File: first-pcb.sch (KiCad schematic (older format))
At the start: 14 parts

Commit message: Electronic schematic is over
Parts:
- added D1, D2, D3, D4: D_Small, Diode_SMD:D_SOD-123, symbol Device:D_Small
- added F1: 500mA, Fuse:Fuse_1206_3216Metric, symbol Device:Polyfuse
- added MX1, MX2, MX3, MX4: MX-NoLED, MX_Alps_Hybrid:MX-1U-NoLED, symbol MX_Alps_Hybrid:MX-NoLED
- added USB1: Molex-0548190589, random-keyboard-parts:Molex-0548190589, symbol random-keyboard-parts:Molex-0548190589
- C1, C2, C3, C4, C5, C6: renamed from C?; footprint (none) -> Capacitor_SMD:C_0805_2012Metric
- C7: renamed from C?; footprint (none) -> Diode_SMD:D_SOD-123
- R1, R2, R3, R4: renamed from R?; footprint (none) -> Resistor_SMD:R_0805_2012Metric
- SW1: renamed from SW?; footprint (none) -> random-keyboard-parts:SKQG-1155865
- Y1: renamed from Y?; footprint (none) -> Crystal:Crystal_SMD_3225-4Pin_3.2x2.5mm
- gave numbers to parts that had none: 1
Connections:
- net +5V: now also F1.1
- net D+: now also USB1.3 (D+)
- net D-: now also USB1.4 (D-)
- net GND: now also USB1.1 (GND)
- new net: D1.2 (A), MX1.2 (ROW)
- new net: D3.2 (A), MX3.2 (ROW)
- new net: D2.2 (A), MX2.2 (ROW)
- new net: D4.2 (A), MX4.2 (ROW)
- new net COL0: MX1.1 (COL), MX2.1 (COL)
- new net COL1: MX3.1 (COL), MX4.1 (COL)
- new net ROW0: D1.1 (K), D3.1 (K)
- new net ROW1: D2.1 (K), D4.1 (K)
- new net VCC: F1.2, USB1.5 (VBUS)

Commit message: My very first pcb is over
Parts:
- renumbered D3 to D2, D2 to D3, MX3 to MX2, MX2 to MX3
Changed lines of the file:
@@
 	6550 3600 6700 3600
 $Comp
-L MX_Alps_Hybrid:MX-NoLED MX3
+L MX_Alps_Hybrid:MX-NoLED MX2
 U 1 1 5E8CAD05
 P 7400 3450
-F 0 "MX3" H 7433 3673 60  0000 C CNN
+F 0 "MX2" H 7433 3673 60  0000 C CNN
 F 1 "MX-NoLED" H 7433 3599 20  0000 C CNN
 F 2 "MX_Alps_Hybrid:MX-1U-NoLED" H 6775 3425 60  0001 C CNN
@@
 $EndComp
 $Comp
-L Device:D_Small D3
+L Device:D_Small D2
 U 1 1 5E8CAD0B
 P 7200 3700
-F 0 "D3" V 7246 3630 50  0000 R CNN
+F 0 "D2" V 7246 3630 50  0000 R CNN
 F 1 "D_Small" V 7155 3630 50  0000 R CNN
 F 2 "Diode_SMD:D_SOD-123" V 7200 3700 50  0001 C CNN
@@
 	7200 3600 7350 3600
 $Comp
-L MX_Alps_Hybrid:MX-NoLED MX2
+L MX_Alps_Hybrid:MX-NoLED MX3
 U 1 1 5E8CBEF5
 P 6750 4150
-F 0 "MX2" H 6783 4373 60  0000 C CNN
+F 0 "MX3" H 6783 4373 60  0000 C CNN
 F 1 "MX-NoLED" H 6783 4299 20  0000 C CNN
 F 2 "MX_Alps_Hybrid:MX-1U-NoLED" H 6125 4125 60  0001 C CNN
@@
 $EndComp
 $Comp
-L Device:D_Small D2
+L Device:D_Small D3
 U 1 1 5E8CBEFB
 P 6550 4400
-F 0 "D2" V 6596 4330 50  0000 R CNN
+F 0 "D3" V 6596 4330 50  0000 R CNN
 F 1 "D_Small" V 6505 4330 50  0000 R CNN
 F 2 "Diode_SMD:D_SOD-123" V 6550 4400 50  0001 C CNN

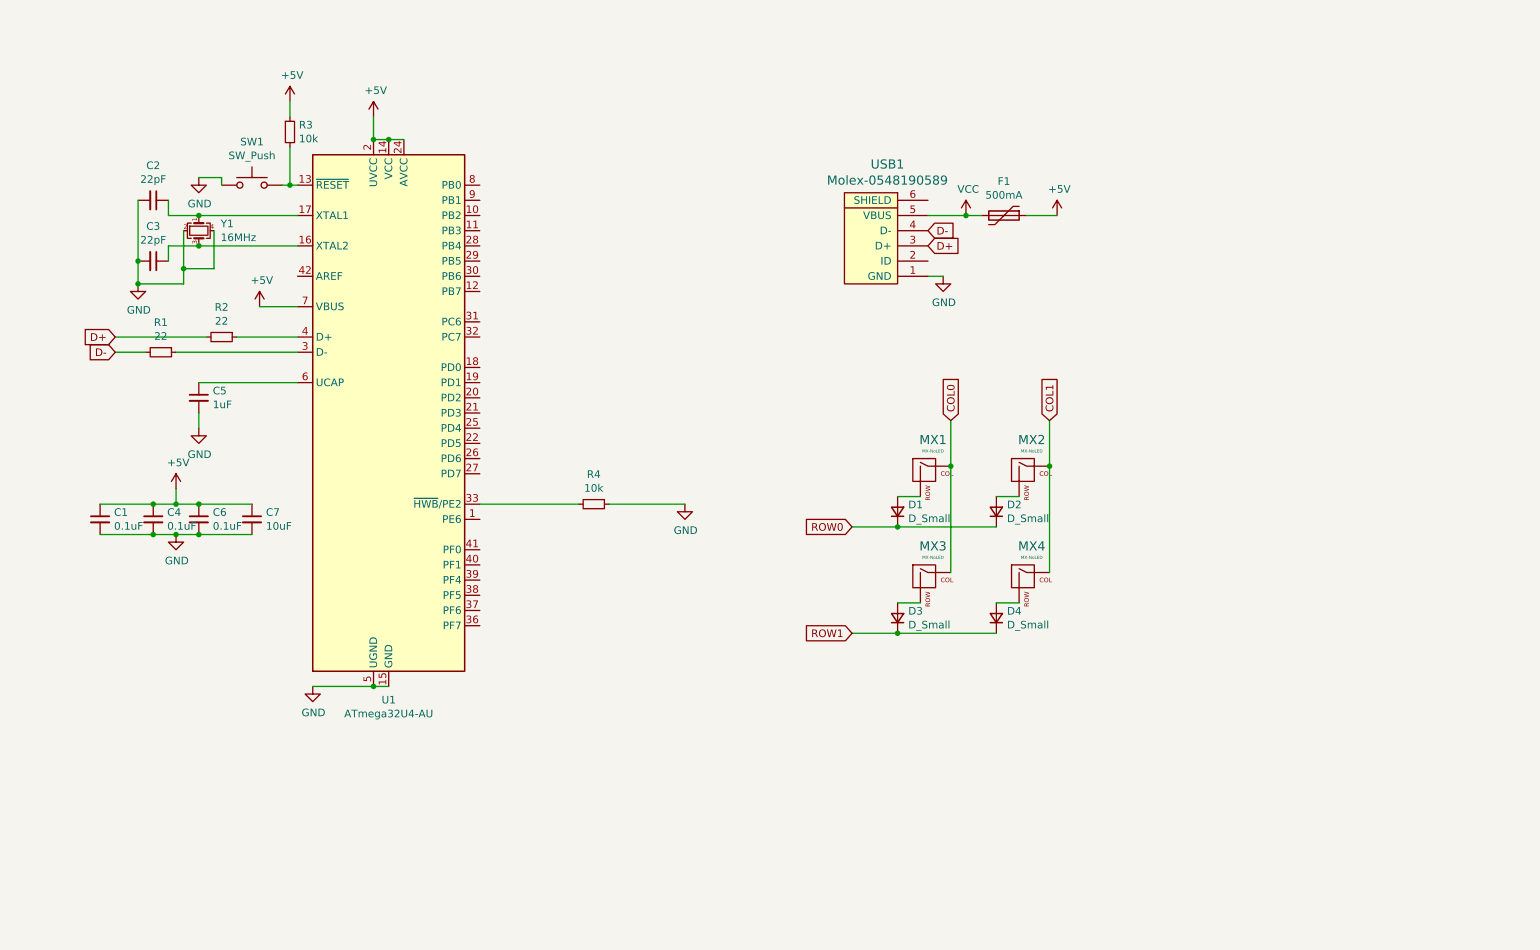
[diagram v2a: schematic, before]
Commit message: First revision (#1)
First design includes 44 switch, 44 smd diodes, 1 pro-micro, 1 4-pin header for oled screen,
outline and mounting points

* V0.0.1 of the flatbrain keyboard

* Replace 1u in thumb by 1.75 and 1.5

* Perfect alignement

* routing corrected

* realign + outline

* add contour.dxf

* final design

* first revision is over
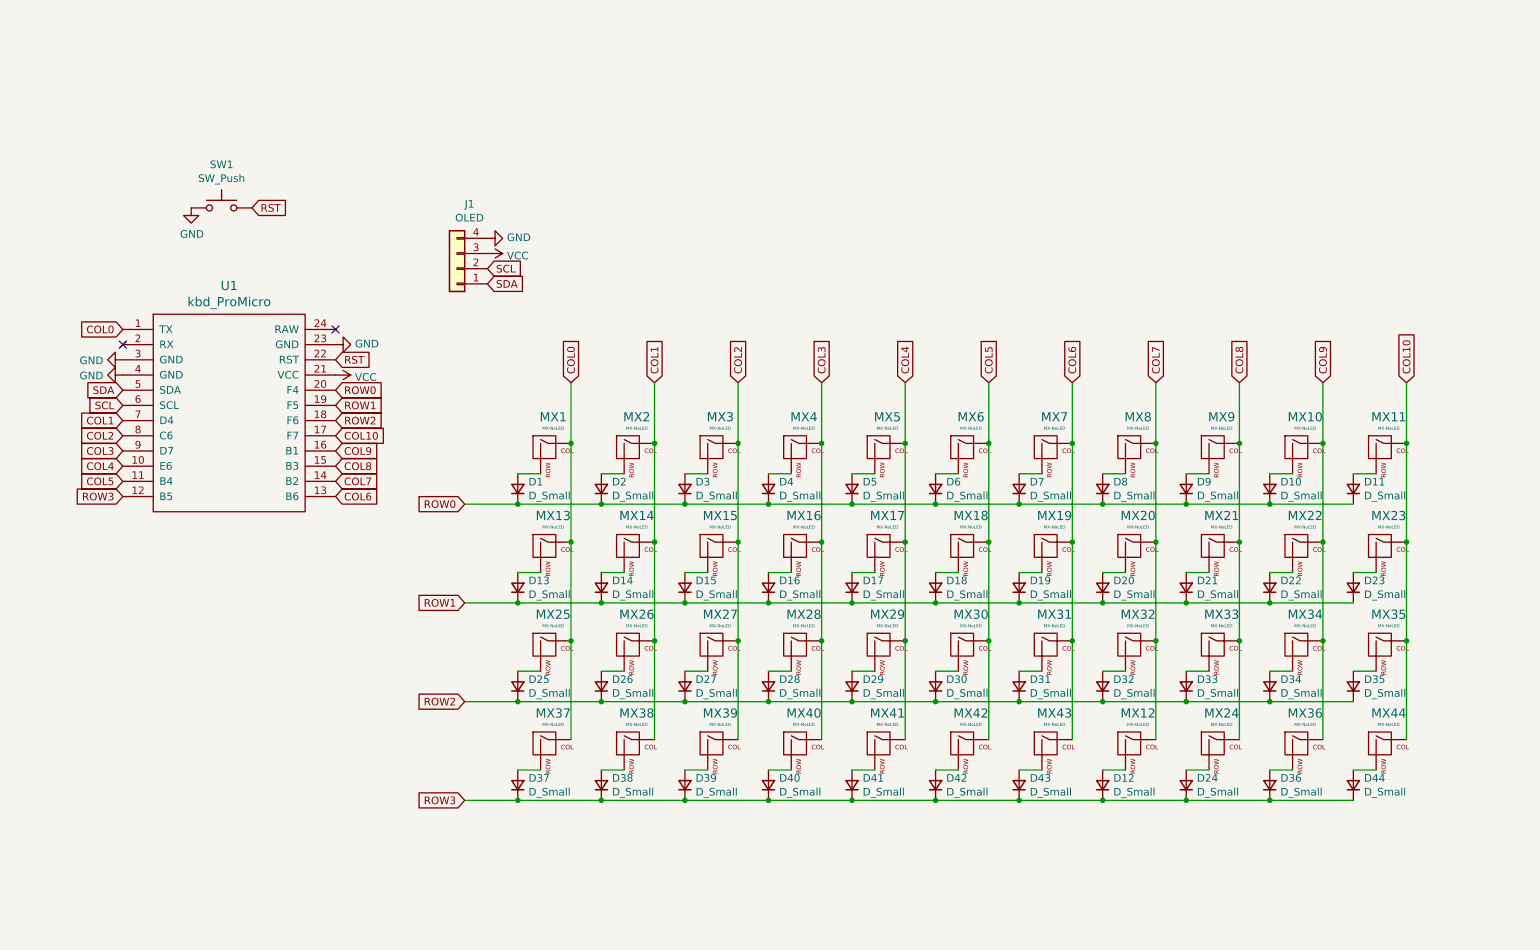
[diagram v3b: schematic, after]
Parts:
- removed C1, C4, C6: 0.1uF, Capacitor_SMD:C_0805_2012Metric, symbol Device:C_Small
- removed C2, C3: 22pF, Capacitor_SMD:C_0805_2012Metric, symbol Device:C_Small
- removed C5: 1uF, Capacitor_SMD:C_0805_2012Metric, symbol Device:C_Small
- removed C7: 10uF, Diode_SMD:D_SOD-123, symbol Device:C_Small
- removed D1: D_Small, Diode_SMD:D_SOD-123, symbol Device:D_Small
- removed F1: 500mA, Fuse:Fuse_1206_3216Metric, symbol Device:Polyfuse
- removed MX1: MX-NoLED, MX_Alps_Hybrid:MX-1U-NoLED, symbol MX_Alps_Hybrid:MX-NoLED
- removed R1, R2: 22, Resistor_SMD:R_0805_2012Metric, symbol Device:R_Small
- removed R3, R4: 10k, Resistor_SMD:R_0805_2012Metric, symbol Device:R_Small
- removed U1: ATmega32U4-AU, Package_QFP:TQFP-44_10x10mm_P0.8mm, symbol MCU_Microchip_ATmega:ATmega32U4-AU
- removed USB1: Molex-0548190589, random-keyboard-parts:Molex-0548190589, symbol random-keyboard-parts:Molex-0548190589
- removed Y1: 16MHz, Crystal:Crystal_SMD_3225-4Pin_3.2x2.5mm, symbol Device:Crystal_GND24_Small
- added D10, D11, D12, D14, D15, D16, D17, D18, D19, D2, D20, D21, D22, D23, D24, D25, D26, D27, D28, D29, D3, D30, D31, D32, D33, D34, D35, D36, D37, D38, D39, D40, D41, D42, D43, D44, D5, D6, D7, D8, D9: D_Small, Diode_SMD:D_SOD-123, symbol Device:D_Small
- added J1: OLED, Connector_PinHeader_2.54mm:PinHeader_1x04_P2.54mm_Vertical, symbol corne-light-cache:Connector_Generic_Conn_01x04
- added MX10, MX11, MX12, MX14, MX15, MX16, MX17, MX18, MX19, MX2, MX20, MX21, MX22, MX23, MX24, MX25, MX26, MX27, MX28, MX29, MX3, MX30, MX31, MX32, MX33, MX34, MX35, MX36, MX37, MX38, MX43, MX44, MX5, MX6, MX7, MX8, MX9: MX-NoLED, MX_Only:MXOnly-1U-NoLED, symbol MX_Alps_Hybrid:MX-NoLED
- added MX39, MX42: MX-NoLED, MX_Only:MXOnly-1.75U-NoLED, symbol MX_Alps_Hybrid:MX-NoLED
- added MX40, MX41: MX-NoLED, MX_Only:MXOnly-1.5U-NoLED, symbol MX_Alps_Hybrid:MX-NoLED
- added U1: kbd_ProMicro, Keebio-Parts:ArduinoProMicro, symbol corne-light-cache:kbd_ProMicro
- MX1: renamed from MX2; footprint MX_Alps_Hybrid:MX-1U-NoLED -> MX_Only:MXOnly-1U-NoLED
- MX13: renamed from MX3; footprint MX_Alps_Hybrid:MX-1U-NoLED -> MX_Only:MXOnly-1U-NoLED
- MX4: footprint MX_Alps_Hybrid:MX-1U-NoLED -> MX_Only:MXOnly-1U-NoLED
- renumbered D2 to D1, D3 to D13
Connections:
- net COL0: now also MX1.1 (COL), MX25.1 (COL), MX37.1 (COL), U1.1 (TX)
- net COL1: now also MX14.1 (COL), MX2.1 (COL), MX26.1 (COL), MX38.1 (COL), U1.7 (D4); no longer MX1.1 (COL), MX4.1 (COL)
- net GND: now also J1.4 (Pin_4), U1.23 (GND), U1.3 (GND), U1.4 (GND)
- net ROW0: now also D4.1 (K), D10.1 (K), D11.1 (K), D2.1 (K), D3.1 (K), D5.1 (K), D6.1 (K), D7.1 (K), D8.1 (K), D9.1 (K), U1.20 (F4)
- net ROW1: now also D14.1 (K), D15.1 (K), D16.1 (K), D17.1 (K), D18.1 (K), D19.1 (K), D20.1 (K), D21.1 (K), D22.1 (K), D23.1 (K), U1.19 (F5); no longer D4.1 (K)
- net VCC: now also J1.3 (Pin_3), U1.21 (VCC)
- net RST: now reaches SW1.2
- net RST: now also U1.22 (RST)
- new net: D2.2 (A), MX2.2 (ROW)
- new net: D3.2 (A), MX3.2 (ROW)
- new net: D14.2 (A), MX14.2 (ROW)
- new net: D15.2 (A), MX15.2 (ROW)
- new net: D5.2 (A), MX5.2 (ROW)
- new net: D16.2 (A), MX16.2 (ROW)
- new net: D17.2 (A), MX17.2 (ROW)
- new net: D25.2 (A), MX25.2 (ROW)
- new net: D26.2 (A), MX26.2 (ROW)
- new net: D27.2 (A), MX27.2 (ROW)
- new net: D28.2 (A), MX28.2 (ROW)
- new net: D29.2 (A), MX29.2 (ROW)
- new net: D30.2 (A), MX30.2 (ROW)
- new net: D6.2 (A), MX6.2 (ROW)
- new net: D18.2 (A), MX18.2 (ROW)
- new net: D37.2 (A), MX37.2 (ROW)
- new net: D38.2 (A), MX38.2 (ROW)
- new net: D39.2 (A), MX39.2 (ROW)
- new net: D40.2 (A), MX40.2 (ROW)
- new net: D7.2 (A), MX7.2 (ROW)
- new net: D19.2 (A), MX19.2 (ROW)
- new net: D8.2 (A), MX8.2 (ROW)
- new net: D9.2 (A), MX9.2 (ROW)
- new net: D20.2 (A), MX20.2 (ROW)
- new net: D21.2 (A), MX21.2 (ROW)
- new net: D10.2 (A), MX10.2 (ROW)
- new net: D11.2 (A), MX11.2 (ROW)
- new net: D22.2 (A), MX22.2 (ROW)
- new net: D23.2 (A), MX23.2 (ROW)
- new net: D31.2 (A), MX31.2 (ROW)
- new net: D32.2 (A), MX32.2 (ROW)
- new net: D33.2 (A), MX33.2 (ROW)
- new net: D34.2 (A), MX34.2 (ROW)
- new net: D35.2 (A), MX35.2 (ROW)
- new net: D36.2 (A), MX36.2 (ROW)
- new net: D12.2 (A), MX12.2 (ROW)
- new net: D24.2 (A), MX24.2 (ROW)
- new net: D41.2 (A), MX41.2 (ROW)
- new net: D42.2 (A), MX42.2 (ROW)
- new net: D43.2 (A), MX43.2 (ROW)
- new net: D44.2 (A), MX44.2 (ROW)
- new net COL10: MX11.1 (COL), MX23.1 (COL), MX35.1 (COL), MX44.1 (COL), U1.17 (F7)
- new net COL2: MX15.1 (COL), MX27.1 (COL), MX3.1 (COL), MX39.1 (COL), U1.8 (C6)
- new net COL3: MX16.1 (COL), MX28.1 (COL), MX4.1 (COL), MX40.1 (COL), U1.9 (D7)
- new net COL4: MX17.1 (COL), MX29.1 (COL), MX41.1 (COL), MX5.1 (COL), U1.10 (E6)
- new net COL5: MX18.1 (COL), MX30.1 (COL), MX42.1 (COL), MX6.1 (COL), U1.11 (B4)
- new net COL6: MX19.1 (COL), MX31.1 (COL), MX43.1 (COL), MX7.1 (COL), U1.13 (B6)
- new net COL7: MX12.1 (COL), MX20.1 (COL), MX32.1 (COL), MX8.1 (COL), U1.14 (B2)
- new net COL8: MX21.1 (COL), MX24.1 (COL), MX33.1 (COL), MX9.1 (COL), U1.15 (B3)
- new net COL9: MX10.1 (COL), MX22.1 (COL), MX34.1 (COL), MX36.1 (COL), U1.16 (B1)
- new net ROW2: D25.1 (K), D26.1 (K), D27.1 (K), D28.1 (K), D29.1 (K), D30.1 (K), D31.1 (K), D32.1 (K), D33.1 (K), D34.1 (K), D35.1 (K), U1.18 (F6)
- new net ROW3: D12.1 (K), D24.1 (K), D36.1 (K), D37.1 (K), D38.1 (K), D39.1 (K), D40.1 (K), D41.1 (K), D42.1 (K), D43.1 (K), D44.1 (K), U1.12 (B5)
- new net SCL: J1.2 (Pin_2), U1.6 (SCL)
- new net SDA: J1.1 (Pin_1), U1.5 (SDA)
- no-connect marks 0 -> 2
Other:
- moved on the sheet: D1, D13, MX1, MX13, SW1

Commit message: New routing to use less pin
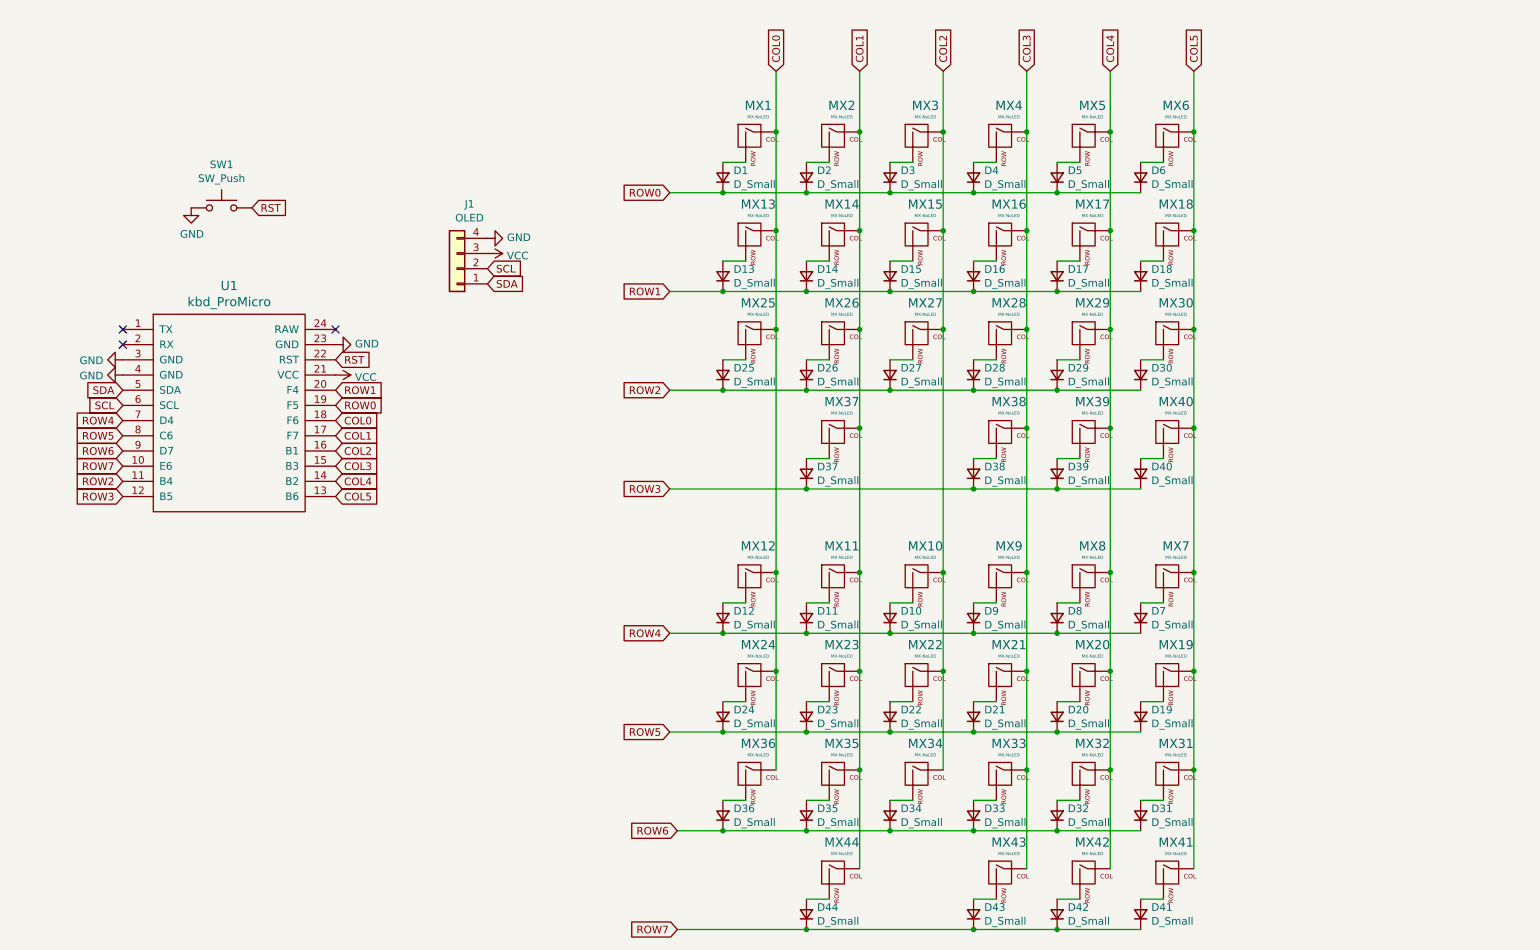
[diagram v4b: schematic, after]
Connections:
- net COL10 is gone; now on net COL1: MX11.1 (COL), MX23.1 (COL), MX35.1 (COL), MX44.1 (COL), U1.17 (F7)
- net COL0: now also MX12.1 (COL), MX24.1 (COL), MX36.1 (COL), U1.18 (F6); no longer MX37.1 (COL), U1.1 (TX)
- net COL1: now also MX37.1 (COL); no longer MX38.1 (COL), U1.7 (D4)
- net COL2: now also MX10.1 (COL), MX22.1 (COL), MX34.1 (COL), U1.16 (B1); no longer MX39.1 (COL), U1.8 (C6)
- net COL3: now also MX21.1 (COL), MX33.1 (COL), MX38.1 (COL), MX43.1 (COL), MX9.1 (COL), U1.15 (B3); no longer MX40.1 (COL), U1.9 (D7)
- net COL4: now also MX20.1 (COL), MX32.1 (COL), MX39.1 (COL), MX42.1 (COL), MX8.1 (COL), U1.14 (B2); no longer MX41.1 (COL), U1.10 (E6)
- net COL5: now also MX19.1 (COL), MX31.1 (COL), MX40.1 (COL), MX41.1 (COL), MX7.1 (COL), U1.13 (B6); no longer MX42.1 (COL), U1.11 (B4)
- net ROW0: now also U1.19 (F5); no longer D10.1 (K), D11.1 (K), D7.1 (K), D8.1 (K), D9.1 (K), U1.20 (F4)
- net ROW1: now also U1.20 (F4); no longer D19.1 (K), D20.1 (K), D21.1 (K), D22.1 (K), D23.1 (K), U1.19 (F5)
- net ROW2: now also U1.11 (B4); no longer D31.1 (K), D32.1 (K), D33.1 (K), D34.1 (K), D35.1 (K), U1.18 (F6)
- net ROW3: no longer D12.1 (K), D24.1 (K), D36.1 (K), D41.1 (K), D42.1 (K), D43.1 (K), D44.1 (K)
- removed net COL6: MX19.1 (COL), MX31.1 (COL), MX43.1 (COL), MX7.1 (COL), U1.13 (B6)
- removed net COL7: MX12.1 (COL), MX20.1 (COL), MX32.1 (COL), MX8.1 (COL), U1.14 (B2)
- removed net COL8: MX21.1 (COL), MX24.1 (COL), MX33.1 (COL), MX9.1 (COL), U1.15 (B3)
- removed net COL9: MX10.1 (COL), MX22.1 (COL), MX34.1 (COL), MX36.1 (COL), U1.16 (B1)
- new net ROW4: D10.1 (K), D11.1 (K), D12.1 (K), D7.1 (K), D8.1 (K), D9.1 (K), U1.7 (D4)
- new net ROW5: D19.1 (K), D20.1 (K), D21.1 (K), D22.1 (K), D23.1 (K), D24.1 (K), U1.8 (C6)
- new net ROW6: D31.1 (K), D32.1 (K), D33.1 (K), D34.1 (K), D35.1 (K), D36.1 (K), U1.9 (D7)
- new net ROW7: D41.1 (K), D42.1 (K), D43.1 (K), D44.1 (K), U1.10 (E6)
- no-connect marks 2 -> 3
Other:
- moved on the sheet: D1, D10, D11, D12, D13, D14, D15, D16, D17, D18, D19, D2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
